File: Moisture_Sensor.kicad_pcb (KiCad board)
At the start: 2 copper layers, 25 x 17 mm, 17 parts, among them J1 UPDI, J2 OLED SSD1306 0.96in, J3 STEMMA QT soil sensor, J5 BATTERY 2xAAA, Q1 DMG3415U, SW1 READ, U1 ATtiny1614-SSNR, U2 TPS22917DBVR

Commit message: Switch OLED connection to 2.54 mm pads matching ELEGOO module (GND-VCC-SCL-SDA)
Co-authored-by: Copilot App <223556219+Copilot@users.noreply.github.com>
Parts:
- J2: footprint Connector_JST:JST_SH_SM04B-SRSS-TB_1x04-1MP_P1.00mm_Horizontal -> Connector_PinHeader_2.54mm:PinHeader_1x04_P2.54mm_Vertical
- moved J2 3.00 mm to (101.8, 101.6), turned to 90 degrees
- moved C4 2.80 mm to (118.4, 102.2)
- moved J1 2.80 mm to (123.4, 109.5)
- moved R3 2.80 mm to (123.4, 109.0)
- moved SW1 2.80 mm to (123.4, 114.6)
- moved U1 2.80 mm to (114.4, 112.2)
- moved C2 2.80 mm to (114.6, 105.6)
- moved C3 2.80 mm to (117.0, 105.6)
- moved C5 2.80 mm to (112.2, 105.6)
- moved C6 2.80 mm to (112.2, 102.2)
- moved J3 2.80 mm to (123.6, 103.4)
- moved R1 2.80 mm to (119.8, 109.0)
- moved R2 2.80 mm to (121.6, 109.0)
- moved U2 2.80 mm to (115.3, 102.2)
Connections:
- J2 pad 3: /SDA -> /SCL
- J2 pad 4: /SCL -> /SDA
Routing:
- net /VBAT: track 50.7 -> 36.7 mm, vias 3 -> 1
- net /GND: track 78.9 -> 86.6 mm, vias 4 -> 2
- net /SDA: track 29.8 -> 37.1 mm, vias 3 -> 2
- net /SCL: track 32.6 -> 30.8 mm, vias 0 -> 3
- net /BTN: track 16.5 -> 14.7 mm, vias 2 -> 0
- net /QOD: track 16.2 -> 14.7 mm, vias 2 -> 4
- net /LOAD_EN: track 7.91 -> 8.95 mm, vias 2 -> 0
- net /VSW: track 42.2 -> 41.3 mm, vias 2 -> 4
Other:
- board size 25 x 17 mm -> 27.8 x 17 mm
- board text added: "C"
- board text added: "D"
- board text added: "G"
- board text added: "SOIL METER rB"
- board text added: "V"
- board text removed: "SOIL METER rA"

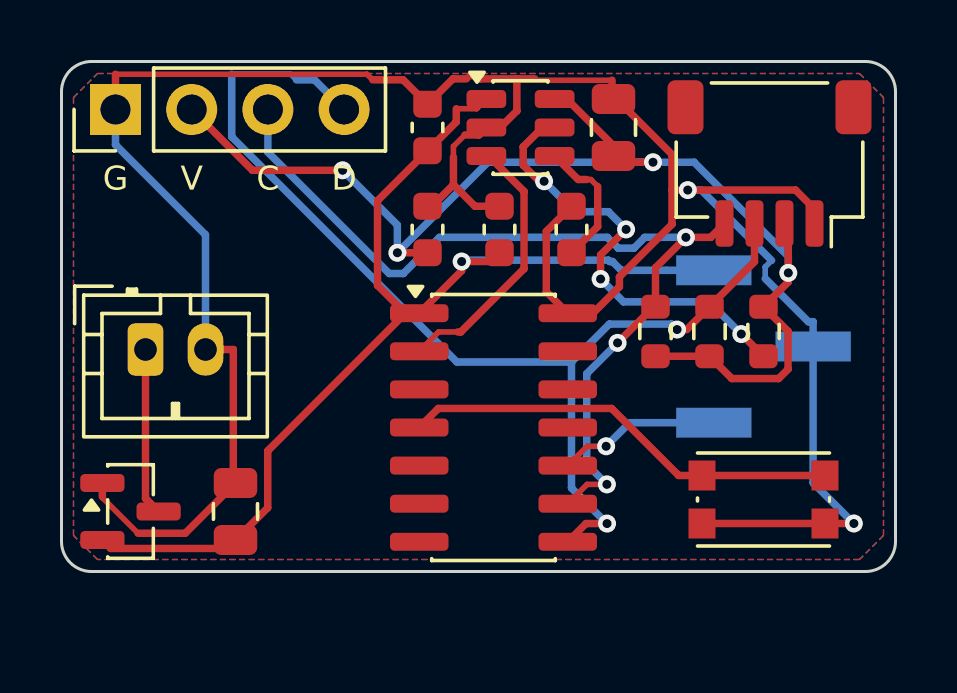
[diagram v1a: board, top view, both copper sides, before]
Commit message: Rev C: 3xAAA, analog soil sensor, panel button, UPDI edge pads; 24x19 mm board
Co-authored-by: Copilot App <223556219+Copilot@users.noreply.github.com>
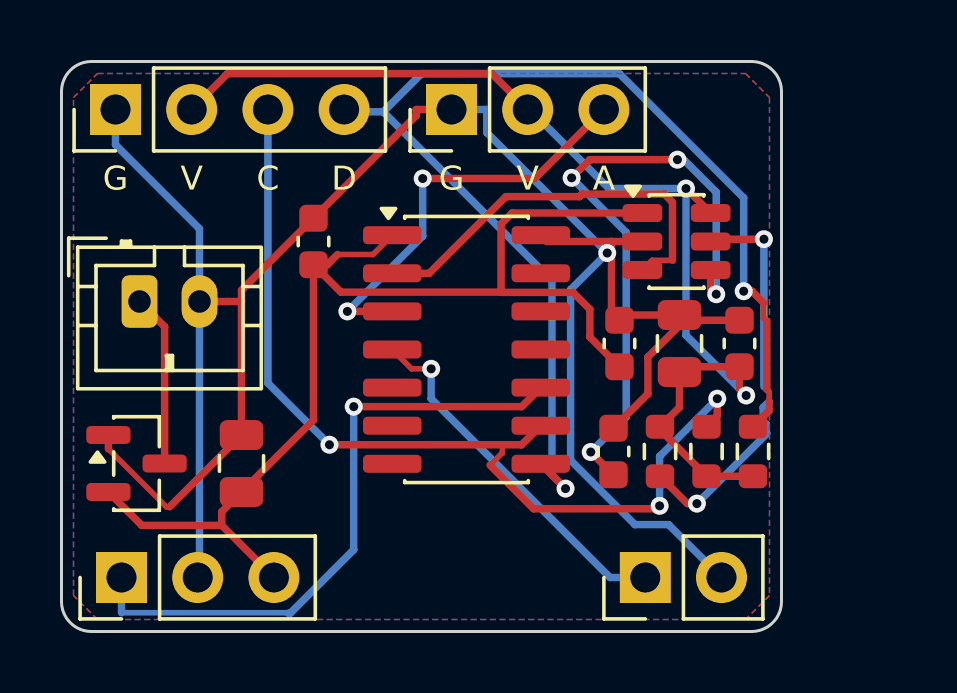
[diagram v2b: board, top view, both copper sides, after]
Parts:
- C4: value 22uF 6.3V X5R -> 22uF 10V X5R
- J1: footprint Connector_PinHeader_2.54mm:PinHeader_1x03_P2.54mm_Vertical_SMD_Pin1Left -> Connector_PinHeader_2.54mm:PinHeader_1x03_P2.54mm_Vertical; moved to F.Cu
- J3: value STEMMA QT soil sensor -> SOIL SENSOR v1.2; footprint Connector_JST:JST_SH_SM04B-SRSS-TB_1x04-1MP_P1.00mm_Horizontal -> Connector_PinHeader_2.54mm:PinHeader_1x03_P2.54mm_Vertical
- J5: value BATTERY 2xAAA -> BATTERY 3xAAA
- SW1: value READ -> READ BUTTON; footprint Button_Switch_SMD:SW_Push_1P1T_NO_CK_KMR2 -> Connector_PinHeader_2.54mm:PinHeader_1x02_P2.54mm_Vertical
- moved J1 22.7 mm to (102.0, 117.2), turned to 90 degrees
- moved C5 11.1 mm to (122.6, 109.4)
- moved J3 10.8 mm to (113.0, 101.6), turned to 90 degrees
- moved C6 9.63 mm to (118.6, 109.4)
- moved C3 7.53 mm to (118.4, 113.0)
- moved C4 7.53 mm to (120.6, 109.4)
- moved U2 6.44 mm to (120.5, 106.0)
- moved C2 6.21 mm to (108.4, 106.0)
- moved R3 5.28 mm to (120.0, 113.0)
- moved SW1 4.72 mm to (119.5, 117.2), turned to 90 degrees
- moved R1 4.35 mm to (121.5, 113.0)
- moved R2 4.25 mm to (123.0, 113.0)
- moved U1 2.75 mm to (113.5, 109.6)
- moved C1 1.61 mm to (106.0, 113.4)
- moved J5 1.61 mm to (102.6, 108.0)
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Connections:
- J3 pad 3: /SDA -> /AOUT
- U1 pad 3: unconnected-(U1-PA5-Pad3) -> /AOUT
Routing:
- net /CT: track 4.43 -> 21.3 mm, vias 0 -> 4
- net /UPDI: track 5.46 -> 21.1 mm
- net /AOUT: track 0.00 -> 14.0 mm, vias 0 -> 2
- net /GND: track 86.6 -> 76.1 mm, vias 2 -> 1
- net /VSW: track 41.3 -> 36.5 mm, vias 4 -> 2
- net /LOAD_EN: track 8.95 -> 13.6 mm
- net /SDA: track 37.1 -> 40.2 mm
- net /BTN: track 14.7 -> 12.2 mm, vias 0 -> 1
- net /VBAT: track 36.7 -> 39.0 mm, vias 1 -> 0
- net /QOD: track 14.7 -> 13.4 mm, vias 4 -> 2
- net /SCL: track 30.8 -> 31.9 mm
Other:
- board size 27.8 x 17 mm -> 24 x 19 mm
- board text added: "A"
- board text added: "BATT +"
- board text added: "BTN"
- board text added: "SOIL METER rC"
- board text added: "U"
- board text removed: "BATT"
- board text removed: "SOIL METER rB"
